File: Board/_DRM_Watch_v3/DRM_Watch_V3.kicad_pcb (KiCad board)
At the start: 2 copper layers, 62.7 x 44.4 mm, 106 parts, among them J1 TYPE-C-31-M-12, J2 687110149022, Q1 2N7002LT1G, U1 ESP32-S2, U3 TP4056, U4 DS3231S, Y1 XRCGB48M000F0Z00R0

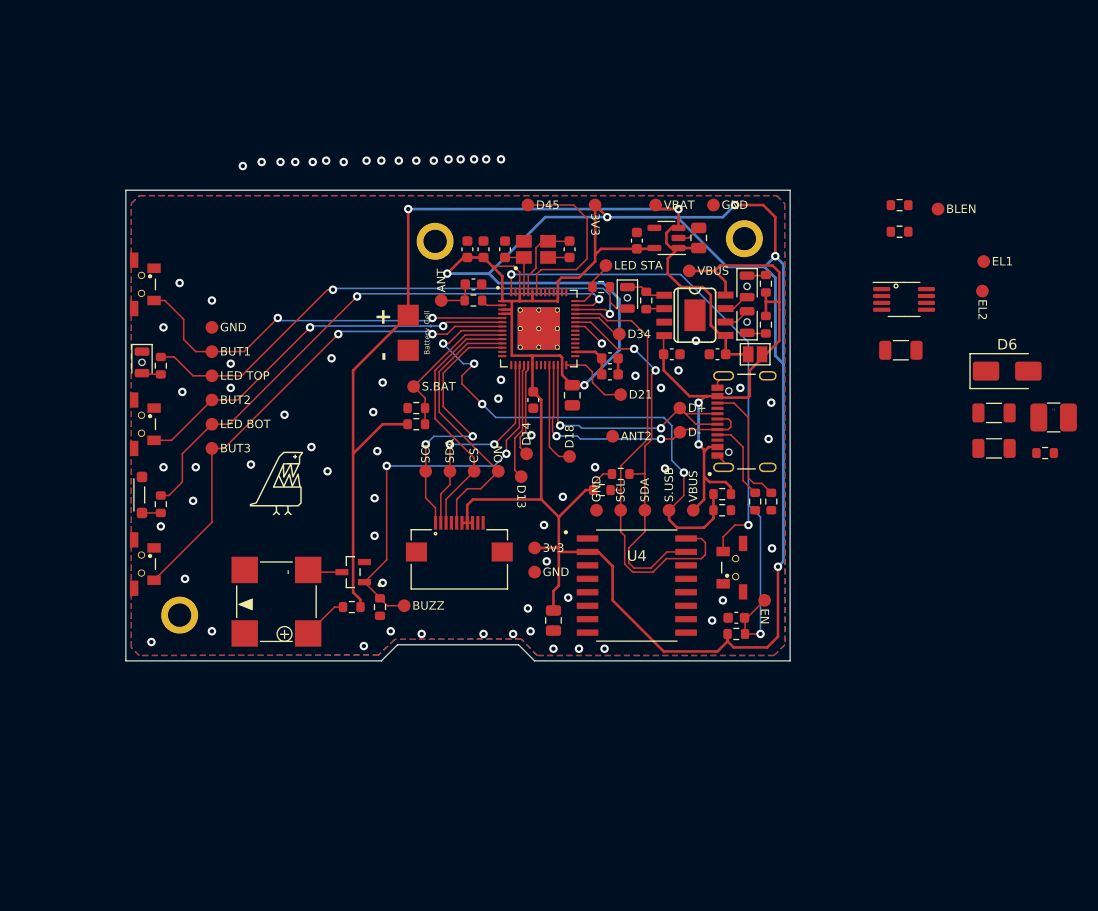
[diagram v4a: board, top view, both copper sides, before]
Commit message: 2024-02-27 Board: Destroyed all the board wiring and start over.
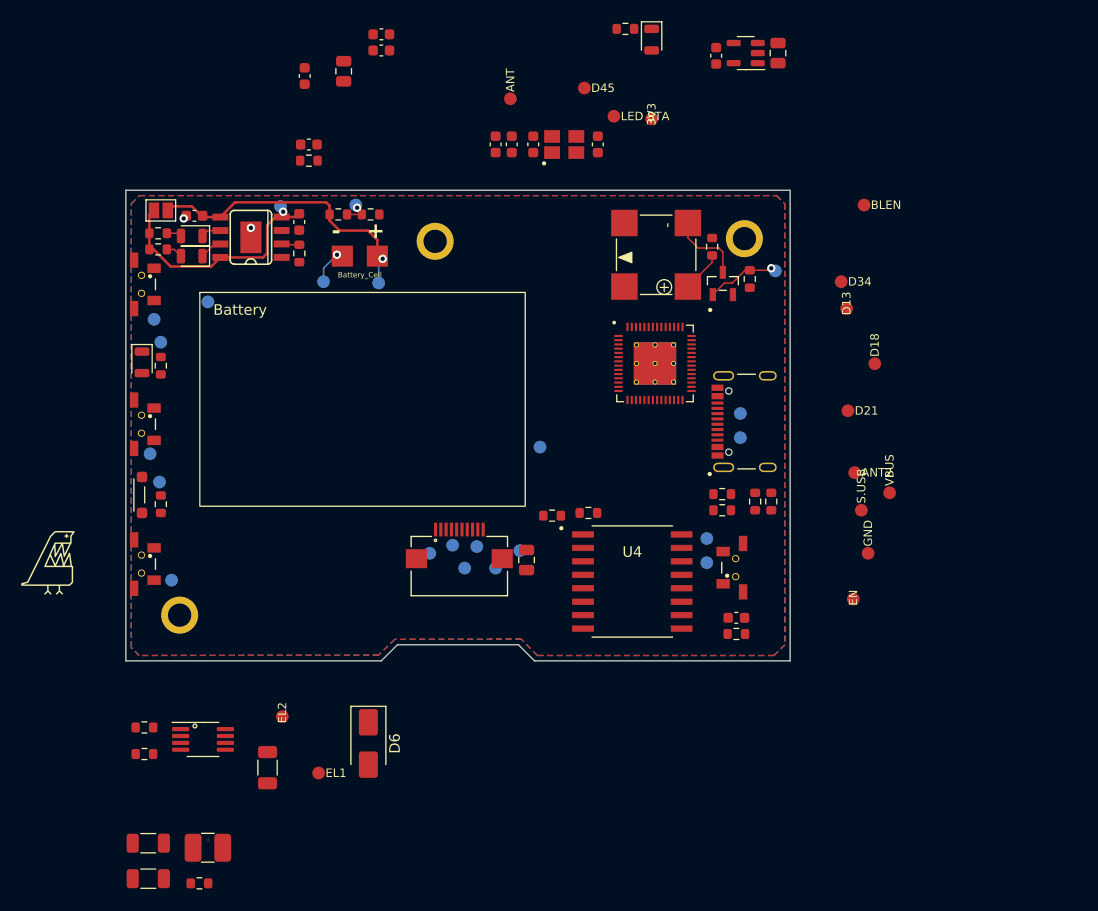
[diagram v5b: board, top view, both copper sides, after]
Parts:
- added REF**: Battery502535, Project-Lib:Battery502535, F.Cu at (88.4, 61.8)
- JP1: value Jumper_2_Open -> Connect this to directly power VCC from USB
- TP11, TP13, TP14, TP15, TP16, TP17, TP18, TP19, TP2, TP20, TP22, TP23, TP24, TP25, TP29, TP3, TP30, TP31, TP4, TP5, TP8, TP9: moved to B.Cu
- moved C17 89.6 mm to (68.2, 104.9)
- moved C18 89.6 mm to (68.2, 108.2)
- moved L1 89.6 mm to (73.8, 105.3)
- moved R21 89.6 mm to (73.0, 108.6)
- moved R17 86.7 mm to (67.8, 93.9)
- moved R18 86.7 mm to (67.8, 96.4)
- moved TP26 79.3 mm to (84.2, 98.2)
- moved U5 78.2 mm to (73.3, 95.1)
- moved TP32 77.4 mm to (80.8, 92.9)
- moved C16 71.6 mm to (79.4, 97.7), turned to -90 degrees
- moved D6 69.8 mm to (88.9, 95.4), turned to -90 degrees
- moved R7 58.0 mm to (69.1, 47.2), turned to 0 degrees
- moved JP1 57.8 mm to (69.3, 45.1), turned to 0 degrees
- moved R8 57.5 mm to (69.1, 48.8), turned to 0 degrees
- moved D3 53.1 mm to (72.3, 47.5), turned to 180 degrees
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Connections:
- R7 pad 2: Net-(D3-K) -> Net-(D3-A)
- R8 pad 2: Net-(D4-K) -> Net-(D4-A)
- U3 pad 6: Net-(D3-A) -> Net-(D3-K)
- U3 pad 7: Net-(D4-A) -> Net-(D4-K)
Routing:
- net +3V3: track 247.1 -> 0.00 mm, vias 6 -> 0
- net VCC: track 97.8 -> 28.0 mm, vias 2 -> 1
- net Net-(U1-CHIP_PU/RESET): track 66.5 -> 0.00 mm, vias 3 -> 0
- net Net-(U1-GPIO37): track 53.6 -> 0.00 mm, vias 2 -> 0
- net Net-(U1-GPIO36): track 52.1 -> 0.00 mm, vias 2 -> 0
- net Net-(U1-GPIO3/ADC1_CH2): track 50.7 -> 0.00 mm, vias 4 -> 0
- net Net-(U1-GPIO2/ADC1_CH1): track 47.1 -> 0.00 mm, vias 2 -> 0
- net Net-(U1-GPIO35): track 43.1 -> 0.00 mm
- net Net-(U1-GPIO0/BOOT): track 37.5 -> 0.00 mm, vias 2 -> 0
- net Net-(U1-GPIO1/ADC1_CH0): track 37.5 -> 0.00 mm, vias 2 -> 0
- net Net-(U1-GPIO33): track 36.4 -> 0.00 mm, vias 2 -> 0
- net VBUS: track 57.9 -> 23.5 mm, vias 2 -> 1
- net Net-(U1-GPIO12/ADC2_CH1): track 37.2 -> 7.04 mm, vias 2 -> 1
- net Net-(U1-GPIO7/ADC1_CH6): track 26.3 -> 0.00 mm, vias 2 -> 0
- net Net-(J1-DP1): track 26.0 -> 0.00 mm, vias 2 -> 0
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
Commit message: 2024-02-27 Board: Moved elements and more wiring
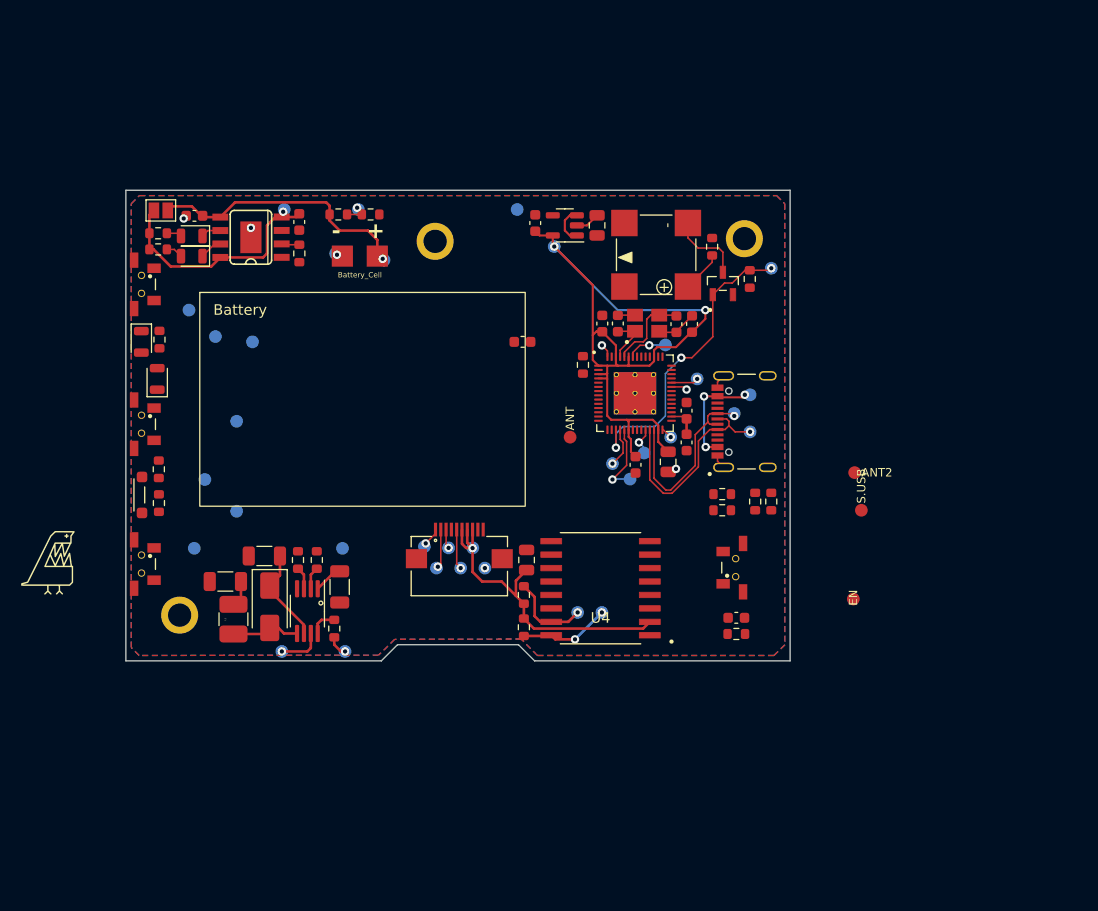
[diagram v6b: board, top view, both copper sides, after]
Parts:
- D6: footprint Diode_SMD:D_SMA -> Project-Lib:US1D
- TP1, TP21, TP26, TP32, TP33, TP34, TP35, TP36, TP37, TP38, TP6, TP7: moved to B.Cu
- moved R10 60.6 mm to (69.2, 69.5), turned to -90 degrees
- moved TP38 59.0 mm to (86.5, 77.0), turned to 90 degrees
- moved D5 56.6 mm to (69.0, 61.0), turned to 90 degrees
- moved TP21 51.7 mm to (73.5, 70.5), turned to 90 degrees
- moved C4 48.2 mm to (114.2, 69.1)
- moved C1 48.0 mm to (117.3, 68.8)
- moved C8 46.9 mm to (119.0, 67.0), turned to -90 degrees
- moved TP6 46.4 mm to (103.0, 45.0), turned to -90 degrees
- moved C7 45.8 mm to (119.0, 64.0), turned to 90 degrees
- moved C18 33.0 mm to (86.2, 80.6), turned to -90 degrees
- moved TP27 32.4 mm to (108.0, 66.5)
- moved R15 32.3 mm to (109.2, 59.7), turned to -90 degrees
- moved C13 27.5 mm to (103.5, 57.5)
- moved R21 27.2 mm to (85.7, 84.6), turned to 90 degrees
- moved TP37 26.5 mm to (112.0, 69.0)
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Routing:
- net +3V3: track 0.00 -> 104.7 mm, vias 0 -> 3
- net Net-(U1-GPIO12/ADC2_CH1): track 7.04 -> 29.3 mm, vias 1 -> 3
- net Net-(J1-DN1): track 0.00 -> 20.6 mm, vias 0 -> 1
- net Net-(J1-DP1): track 0.00 -> 19.0 mm, vias 0 -> 1
- net VBUS: track 23.5 -> 33.9 mm, vias 1 -> 4
- net Net-(U1-GPIO33): track 0.00 -> 9.43 mm, vias 0 -> 2
- net Net-(D6-K): track 0.00 -> 9.06 mm
- net Net-(U1-GPIO35): track 0.00 -> 8.60 mm, vias 0 -> 2
- net Net-(U1-XTAL_N): track 0.00 -> 7.89 mm
- net Net-(U1-GPIO14/ADC2_CH3): track 0.00 -> 7.55 mm, vias 0 -> 1
- net GND: track 3.07 -> 10.5 mm, vias 3 -> 5
- net Net-(D6-A): track 0.00 -> 6.47 mm
- net Net-(U1-XTAL_P): track 0.00 -> 5.15 mm
- net Net-(U5-VB): track 0.00 -> 4.25 mm, vias 0 -> 1
- net Net-(U1-GPIO11/ADC2_CH0): track 0.00 -> 3.81 mm, vias 0 -> 1
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
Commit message: 2024-02-29 move led-charging to edge and make lightpipe for it  2024-02-29 move led-status to edge and make lightpipe for it 2024-02-29 board: Add EL backlight 2024-02-29 Board: move elements to make compact
2024-02-29 move led-charging to edge and make lightpipe for it
2024-02-29 move led-status to edge and make lightpipe for it
2024-02-29 board: Add EL backlight
2024-02-29 Board: move elements to make compact
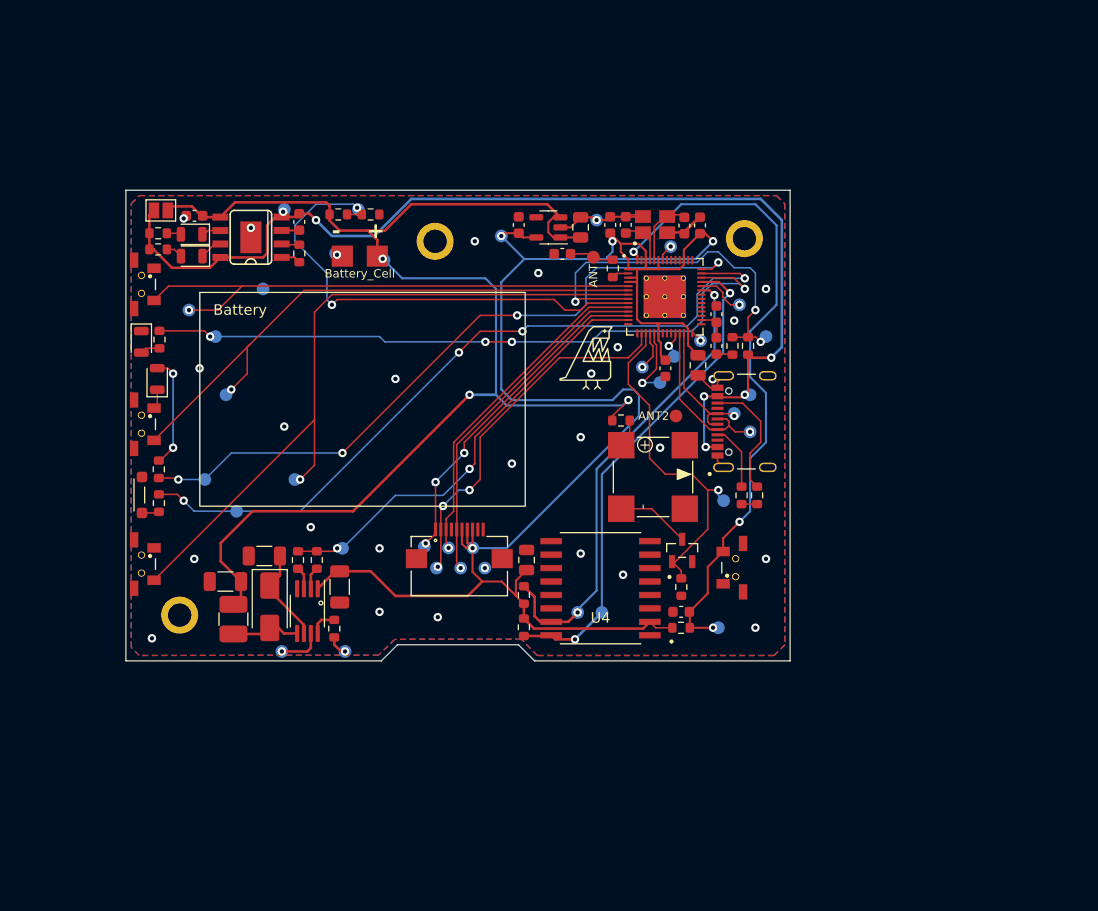
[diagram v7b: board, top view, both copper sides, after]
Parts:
- TP10, TP12: moved to B.Cu
- moved G*** 54.4 mm to (109.5, 59.0)
- moved R1 29.8 mm to (118.5, 80.7)
- moved Q1 25.5 mm to (118.6, 77.2)
- moved TP22 22.4 mm to (122.5, 72.5), turned to -90 degrees
- moved TP12 18.7 mm to (126.5, 57.0)
- moved R4 18.5 mm to (112.8, 64.9), turned to 180 degrees
- moved LS1 18.1 mm to (114.8, 68.7), turned to -90 degrees
- moved TP28 17.7 mm to (118.0, 64.5), turned to 180 degrees
- moved TP27 17.1 mm to (110.2, 49.5), turned to -90 degrees
- moved R14 15.6 mm to (123.3, 57.9), turned to -90 degrees
- moved R13 14.2 mm to (124.8, 57.9), turned to 90 degrees
- moved TP10 13.0 mm to (122.0, 84.5), turned to 90 degrees
- moved TP5 11.5 mm to (82.0, 70.5)
- moved TP31 9.54 mm to (116.5, 61.4)
- moved C4 9.54 mm to (117.0, 60.0)
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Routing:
- net VCC: track 31.6 -> 126.8 mm, vias 1 -> 3
- net Net-(U1-GPIO37): track 0.00 -> 70.6 mm, vias 0 -> 4
- net Net-(U1-GPIO2/ADC1_CH1): track 0.00 -> 68.6 mm, vias 0 -> 1
- net VBUS: track 33.9 -> 102.4 mm, vias 4 -> 6
- net Net-(U1-GPIO38): track 0.00 -> 64.7 mm, vias 0 -> 4
- net Net-(U1-GPIO36): track 0.00 -> 64.3 mm, vias 0 -> 4
- net +3V3: track 104.7 -> 167.8 mm, vias 3 -> 4
- net Net-(U1-CHIP_PU/RESET): track 1.29 -> 62.5 mm, vias 1 -> 3
- net Net-(U1-GPIO1/ADC1_CH0): track 0.00 -> 56.3 mm, vias 0 -> 1
- net Net-(U1-GPIO0/BOOT): track 0.00 -> 51.3 mm, vias 0 -> 1
- net Net-(U1-GPIO4/ADC1_CH3): track 2.52 -> 47.2 mm, vias 1 -> 2
- net Net-(U1-GPIO8/ADC1_CH7): track 0.00 -> 41.7 mm, vias 0 -> 2
- net Net-(U1-GPIO35): track 8.60 -> 46.9 mm
- net Net-(U1-GPIO3/ADC1_CH2): track 0.00 -> 36.4 mm, vias 0 -> 3
- net Net-(U1-GPIO33): track 9.43 -> 44.6 mm
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
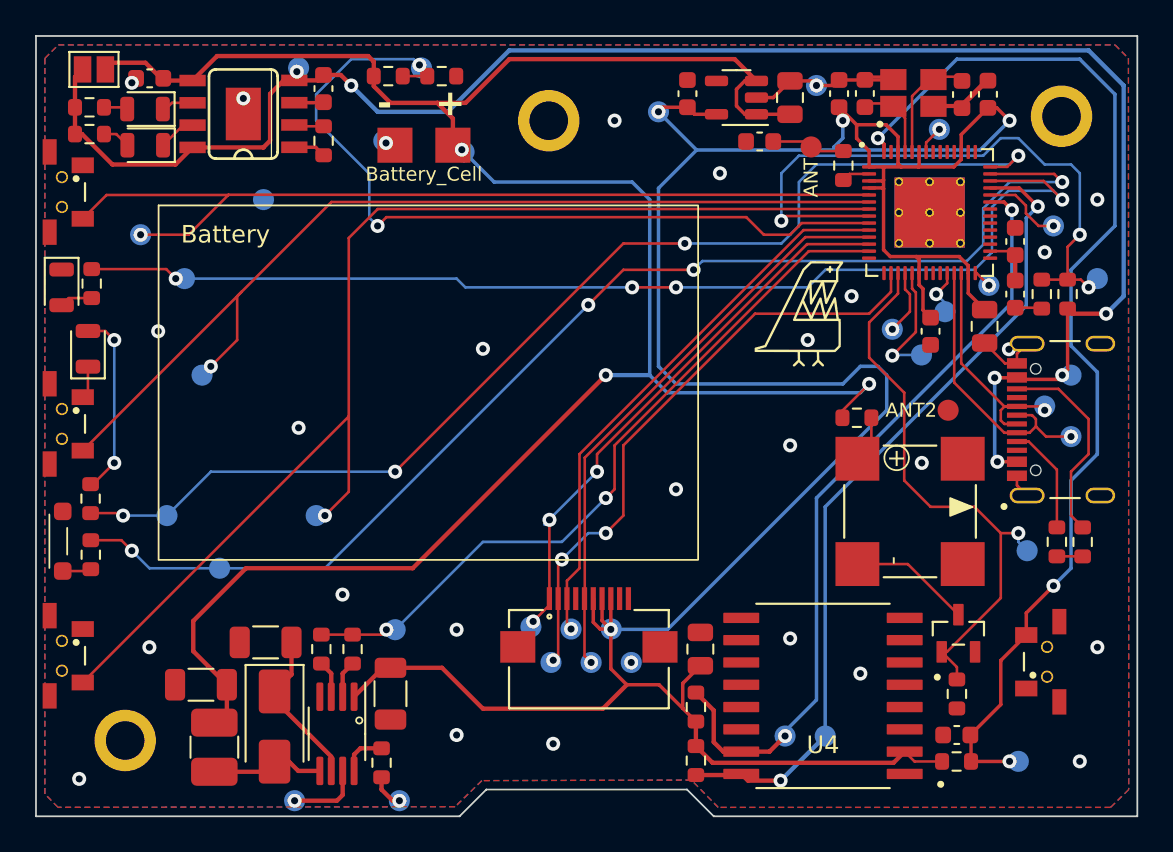
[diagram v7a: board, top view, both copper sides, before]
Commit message: 2024-03-02 Board rev3: add more info to FAB layer to meke it more informative
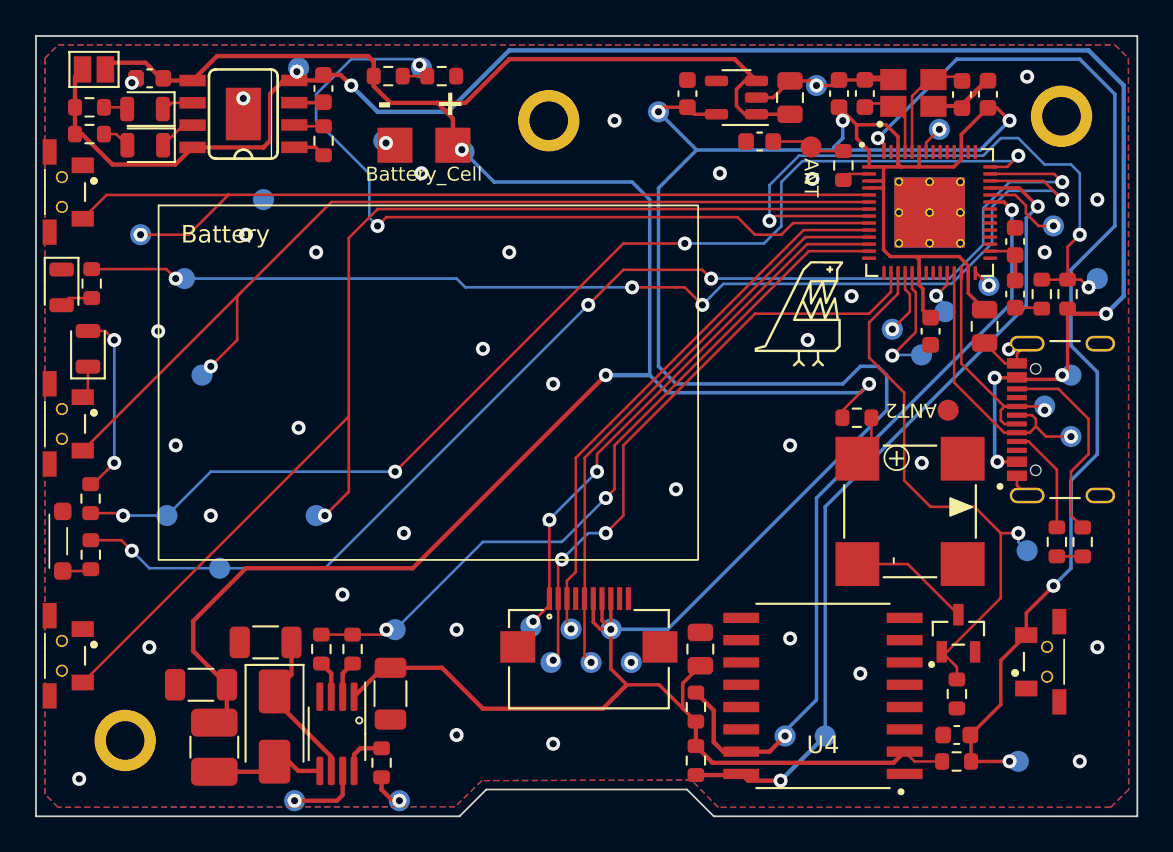
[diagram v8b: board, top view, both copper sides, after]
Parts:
- moved G*** 33.5 mm to (95.0, 59.5)
- moved G*** 32.8 mm to (83.5, 60.5)
- turned TP10 to -90 degrees
- turned TP11 to -90 degrees
- turned TP19 to -90 degrees
- turned TP2 to -90 degrees
- turned TP20 to -90 degrees
- turned TP21 to -90 degrees
- turned TP23 to -90 degrees
- turned TP24 to -90 degrees
- turned TP25 to -90 degrees
- turned TP29 to -90 degrees
- turned TP3 to -90 degrees
- turned TP30 to -90 degrees
- turned TP34 to -90 degrees
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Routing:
- net Net-(U1-GPIO3/ADC1_CH2): track 36.4 -> 37.3 mm
- net Net-(U1-GPIO36): track 64.3 -> 64.8 mm
- net GND: vias 28 -> 38
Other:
- board text added: "Rev.3 (2024-03-02)"
- board text removed: "Rev.2 (2024-01-15)"
